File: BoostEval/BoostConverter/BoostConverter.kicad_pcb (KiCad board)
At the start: 2 copper layers, 58.4 x 13.2 mm, 21 parts, among them J1 Screw_Terminal_01x02, J2 Screw_Terminal_01x02, U1 LMR62421XSD

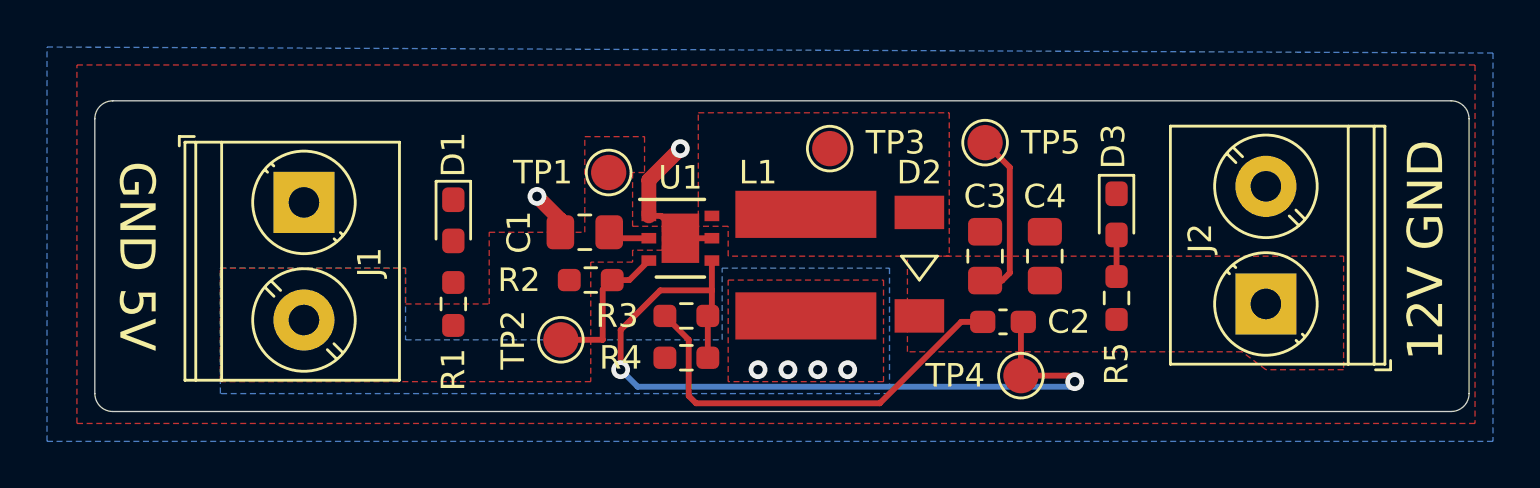
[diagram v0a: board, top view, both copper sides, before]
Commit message: Add in boost Converter and STM32 Breakout
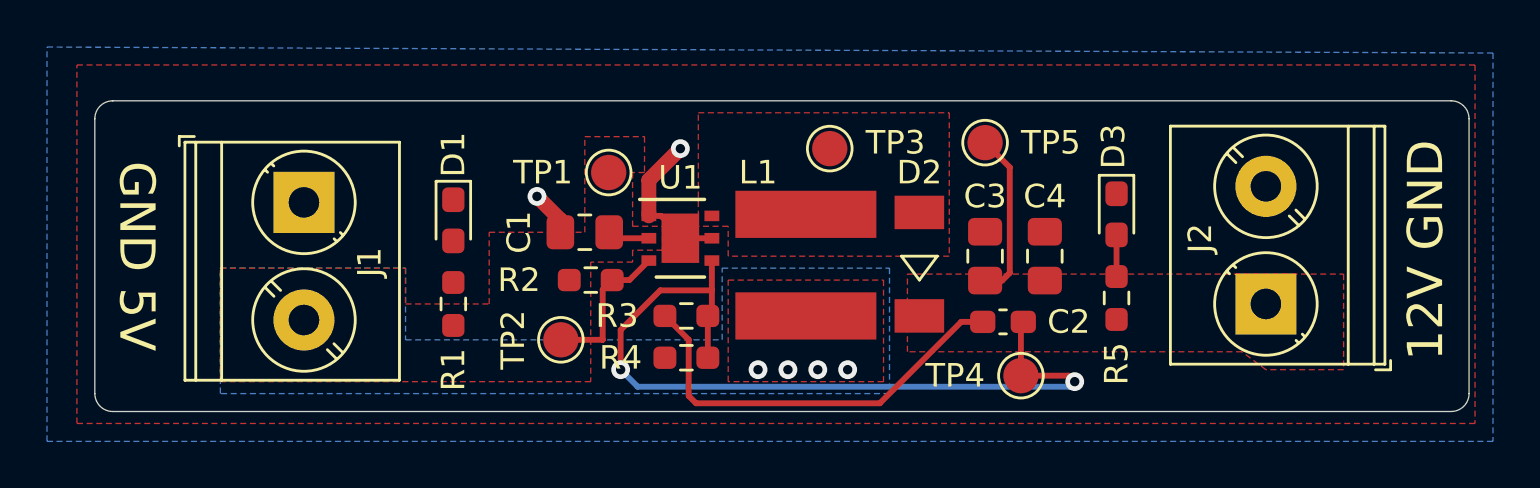
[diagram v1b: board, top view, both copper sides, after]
